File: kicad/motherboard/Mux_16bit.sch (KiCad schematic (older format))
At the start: 13 parts, among them U1 SN74ALVC00, U10 SN74ALVC00, U11 SN74ALVC00, U12 SN74ALVC00, U13 SN74ALVC00, U2 SN74ALVC00, U3 SN74ALVC00, U4 SN74ALVC00, U5 SN74ALVC00, U6 SN74ALVC00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

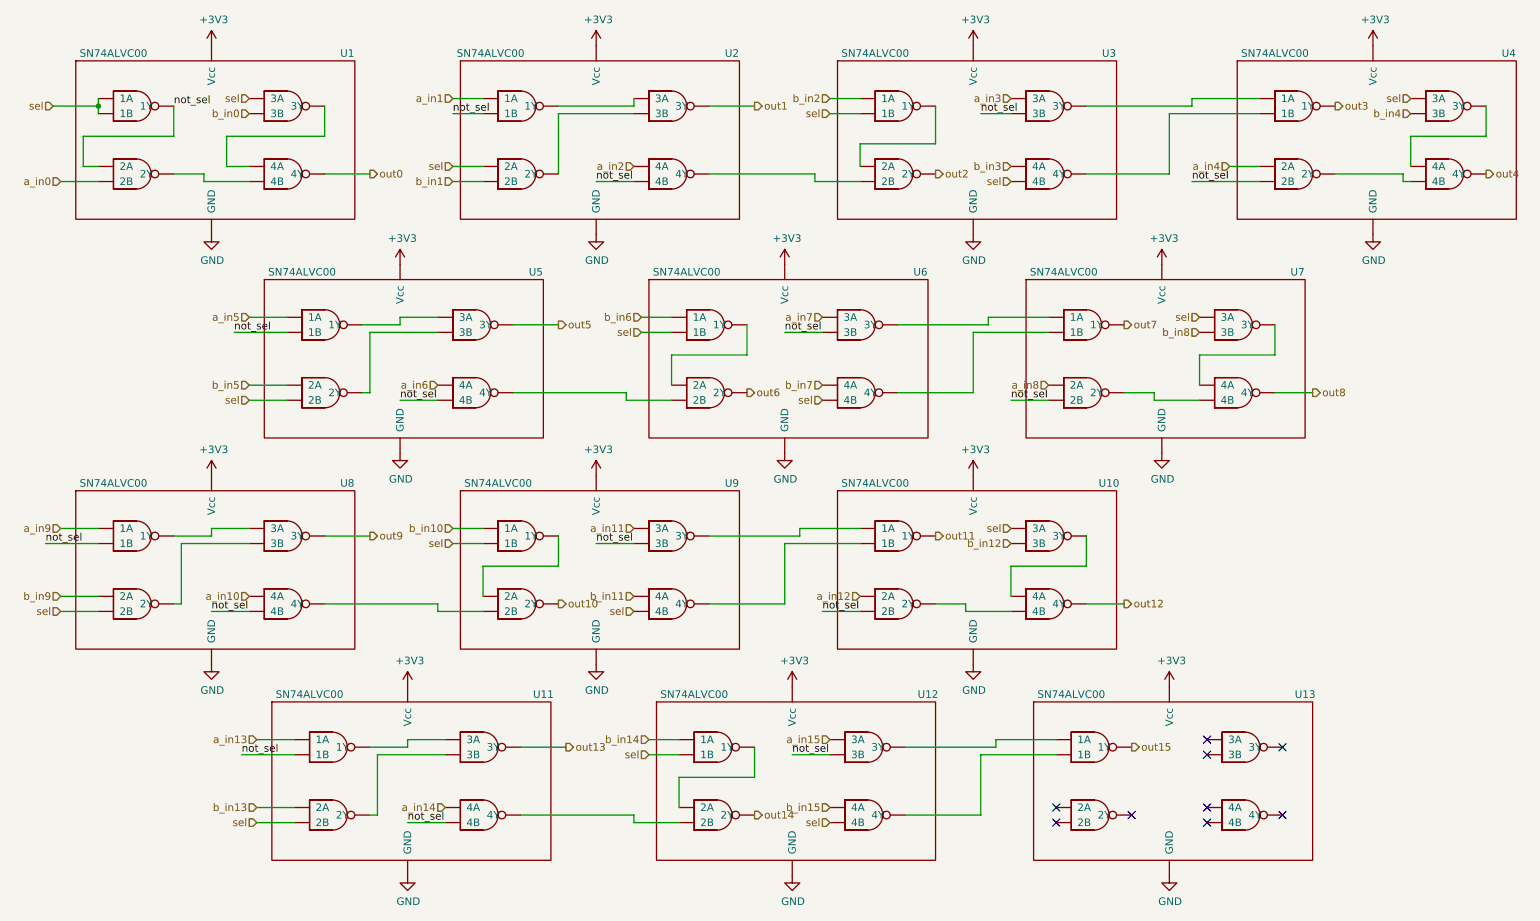
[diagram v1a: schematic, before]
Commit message: Readme updates (#6)
* Readme intro section

* Board revisions for manufacturing, add digikey PNs to all, added logo.
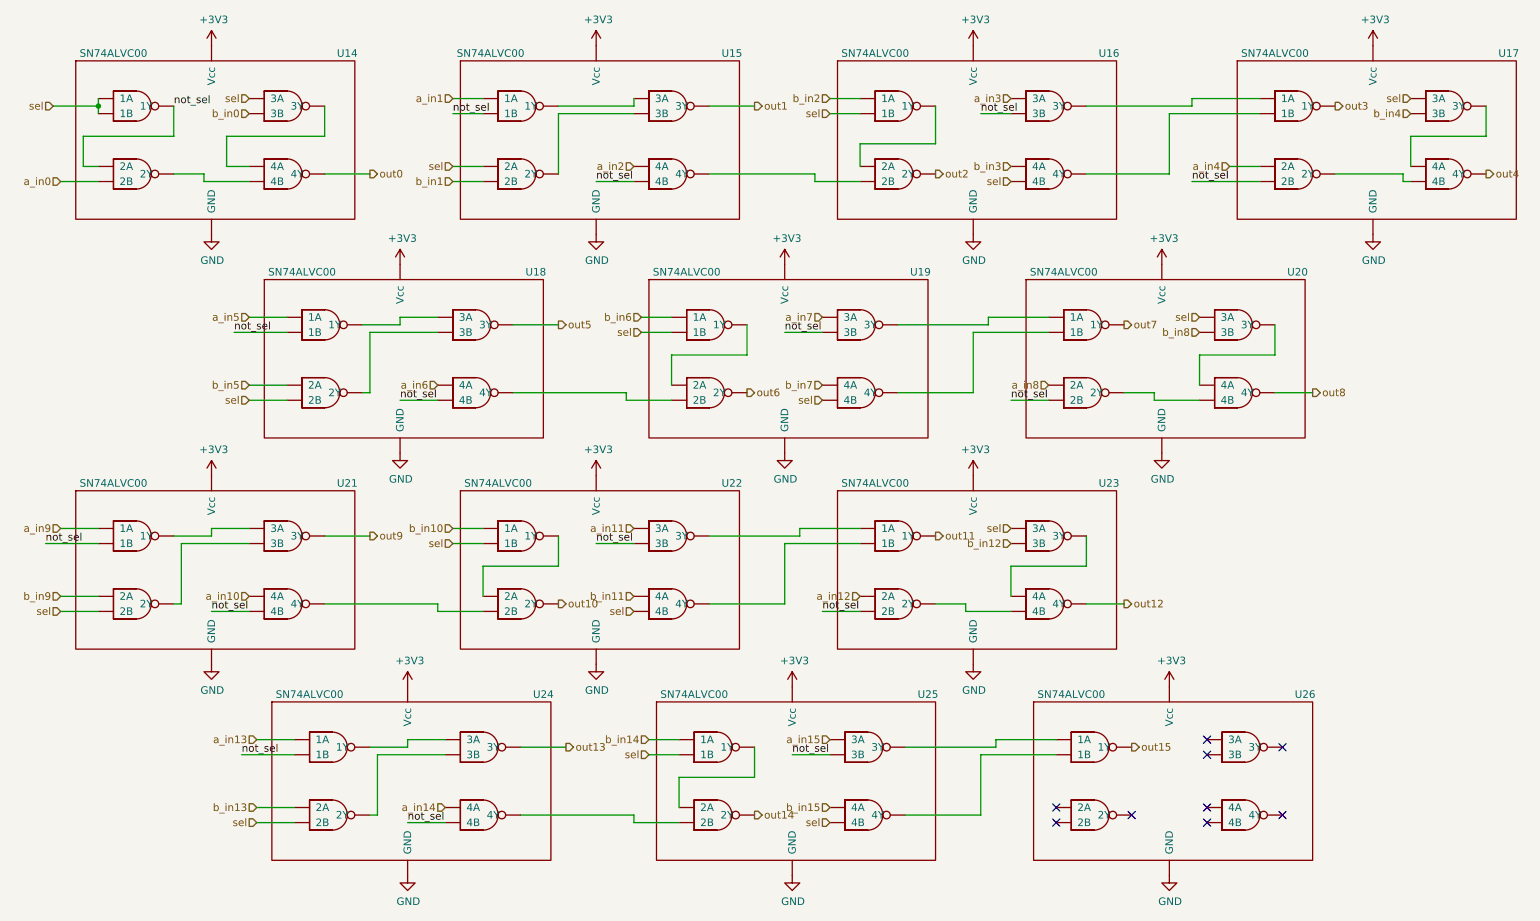
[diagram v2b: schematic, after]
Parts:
- U1, U10, U11, U12, U13, U2, U3, U4, U5, U6, U7, U8, U9: Digikey PN (none) -> 296-5104-1-ND
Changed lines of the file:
@@
 $Descr A4 11693 8268
 encoding utf-8
-Sheet 2 4
+Sheet 3 4
 Title ""
 Date ""
@@
 AR Path="/5E81995D/5E860E76" Ref="U7"  Part="1"
 AR Path="/5EAF9122/5E860E76" Ref="U20"  Part="1"
-F 0 "U7" H 9100 1600 50  0000 C CNN
+F 0 "U20" H 9100 1600 50  0000 C CNN
 F 1 "SN74ALVC00" H 7550 1600 50  0000 C CNN
 F 2 "Package_SO:TSSOP-14_4.4x5mm_P0.65mm" H 8200 450 50  0001 C CNN
 F 3 "" H 8450 1950 50  0001 C CNN
+F 4 "296-5104-1-ND" H 0   0   50  0001 C CNN "Digikey PN"
 	1    8450 1950
 	1    0    0    -1
@@
 AR Path="/5E81995D/5E85FB96" Ref="U6"  Part="1"
 AR Path="/5EAF9122/5E85FB96" Ref="U19"  Part="1"
-F 0 "U6" H 6600 1600 50  0000 C CNN
+F 0 "U19" H 6600 1600 50  0000 C CNN
 F 1 "SN74ALVC00" H 5050 1600 50  0000 C CNN
 F 2 "Package_SO:TSSOP-14_4.4x5mm_P0.65mm" H 5700 450 50  0001 C CNN
 F 3 "" H 5950 1950 50  0001 C CNN
+F 4 "296-5104-1-ND" H 0   0   50  0001 C CNN "Digikey PN"
 	1    5950 1950
 	1    0    0    -1
@@
 AR Path="/5E81995D/5E85D974" Ref="U5"  Part="1"
 AR Path="/5EAF9122/5E85D974" Ref="U18"  Part="1"
-F 0 "U5" H 4050 1600 50  0000 C CNN
+F 0 "U18" H 4050 1600 50  0000 C CNN
 F 1 "SN74ALVC00" H 2500 1600 50  0000 C CNN
 F 2 "Package_SO:TSSOP-14_4.4x5mm_P0.65mm" H 3150 450 50  0001 C CNN
 F 3 "" H 3400 1950 50  0001 C CNN
+F 4 "296-5104-1-ND" H 0   0   50  0001 C CNN "Digikey PN"
 	1    3400 1950
 	1    0    0    -1
@@
 AR Path="/5E81995D/5E835103" Ref="U4"  Part="1"
 AR Path="/5EAF9122/5E835103" Ref="U17"  Part="1"
-F 0 "U4" H 10500 150 50  0000 C CNN
+F 0 "U17" H 10500 150 50  0000 C CNN
 F 1 "SN74ALVC00" H 8950 150 50  0000 C CNN
 F 2 "Package_SO:TSSOP-14_4.4x5mm_P0.65mm" H 9600 -1000 50  0001 C CNN
 F 3 "" H 9850 500 50  0001 C CNN
+F 4 "296-5104-1-ND" H 0   0   50  0001 C CNN "Digikey PN"
 	1    9850 500
 	1    0    0    -1
@@
 AR Path="/5E81995D/5E82D6FB" Ref="U3"  Part="1"
 AR Path="/5EAF9122/5E82D6FB" Ref="U16"  Part="1"
-F 0 "U3" H 7850 150 50  0000 C CNN
+F 0 "U16" H 7850 150 50  0000 C CNN
 F 1 "SN74ALVC00" H 6300 150 50  0000 C CNN
 F 2 "Package_SO:TSSOP-14_4.4x5mm_P0.65mm" H 6950 -1000 50  0001 C CNN
 F 3 "" H 7200 500 50  0001 C CNN
+F 4 "296-5104-1-ND" H 0   0   50  0001 C CNN "Digikey PN"
 	1    7200 500
 	1    0    0    -1
@@
 AR Path="/5E81995D/5E827C09" Ref="U2"  Part="1"
 AR Path="/5EAF9122/5E827C09" Ref="U15"  Part="1"
-F 0 "U2" H 5350 150 50  0000 C CNN
+F 0 "U15" H 5350 150 50  0000 C CNN
 F 1 "SN74ALVC00" H 3750 150 50  0000 C CNN
 F 2 "Package_SO:TSSOP-14_4.4x5mm_P0.65mm" H 4450 -1000 50  0001 C CNN
 F 3 "" H 4700 500 50  0001 C CNN
+F 4 "296-5104-1-ND" H 0   0   50  0001 C CNN "Digikey PN"
 	1    4700 500
 	1    0    0    -1
@@
 AR Path="/5E81995D/5E81C818" Ref="U1"  Part="1"
 AR Path="/5EAF9122/5E81C818" Ref="U14"  Part="1"
-F 0 "U1" H 2800 150 50  0000 C CNN
+F 0 "U14" H 2800 150 50  0000 C CNN
 F 1 "SN74ALVC00" H 1250 150 50  0000 C CNN
 F 2 "Package_SO:TSSOP-14_4.4x5mm_P0.65mm" H 1900 -1000 50  0001 C CNN
 F 3 "" H 2150 500 50  0001 C CNN
+F 4 "296-5104-1-ND" H 0   0   50  0001 C CNN "Digikey PN"
 	1    2150 500
 	1    0    0    -1
@@
 AR Path="/5E81995D/5E98838F" Ref="U10"  Part="1"
 AR Path="/5EAF9122/5E98838F" Ref="U23"  Part="1"
-F 0 "U10" H 7850 3000 50  0000 C CNN
+F 0 "U23" H 7850 3000 50  0000 C CNN
 F 1 "SN74ALVC00" H 6300 3000 50  0000 C CNN
 F 2 "Package_SO:TSSOP-14_4.4x5mm_P0.65mm" H 6950 1850 50  0001 C CNN
 F 3 "" H 7200 3350 50  0001 C CNN
+F 4 "296-5104-1-ND" H 0   0   50  0001 C CNN "Digikey PN"
 	1    7200 3350
 	1    0    0    -1
@@
 AR Path="/5E81995D/5E988395" Ref="U9"  Part="1"
 AR Path="/5EAF9122/5E988395" Ref="U22"  Part="1"
-F 0 "U9" H 5350 3000 50  0000 C CNN
+F 0 "U22" H 5350 3000 50  0000 C CNN
 F 1 "SN74ALVC00" H 3800 3000 50  0000 C CNN
 F 2 "Package_SO:TSSOP-14_4.4x5mm_P0.65mm" H 4450 1850 50  0001 C CNN
 F 3 "" H 4700 3350 50  0001 C CNN
+F 4 "296-5104-1-ND" H 0   0   50  0001 C CNN "Digikey PN"
 	1    4700 3350
 	1    0    0    -1
@@
 AR Path="/5E81995D/5E98839B" Ref="U8"  Part="1"
 AR Path="/5EAF9122/5E98839B" Ref="U21"  Part="1"
-F 0 "U8" H 2800 3000 50  0000 C CNN
+F 0 "U21" H 2800 3000 50  0000 C CNN
 F 1 "SN74ALVC00" H 1250 3000 50  0000 C CNN
 F 2 "Package_SO:TSSOP-14_4.4x5mm_P0.65mm" H 1900 1850 50  0001 C CNN
 F 3 "" H 2150 3350 50  0001 C CNN
+F 4 "296-5104-1-ND" H 0   0   50  0001 C CNN "Digikey PN"
 	1    2150 3350
 	1    0    0    -1
@@
 AR Path="/5E81995D/5E990E7F" Ref="U13"  Part="1"
 AR Path="/5EAF9122/5E990E7F" Ref="U26"  Part="1"
-F 0 "U13" H 9150 4400 50  0000 C CNN
+F 0 "U26" H 9150 4400 50  0000 C CNN
 F 1 "SN74ALVC00" H 7600 4400 50  0000 C CNN
 F 2 "Package_SO:TSSOP-14_4.4x5mm_P0.65mm" H 8250 3250 50  0001 C CNN
 F 3 "" H 8500 4750 50  0001 C CNN
+F 4 "296-5104-1-ND" H 0   0   50  0001 C CNN "Digikey PN"
 	1    8500 4750
 	1    0    0    -1
@@
 AR Path="/5E81995D/5E990E85" Ref="U12"  Part="1"
 AR Path="/5EAF9122/5E990E85" Ref="U25"  Part="1"
-F 0 "U12" H 6650 4400 50  0000 C CNN
+F 0 "U25" H 6650 4400 50  0000 C CNN
 F 1 "SN74ALVC00" H 5100 4400 50  0000 C CNN
 F 2 "Package_SO:TSSOP-14_4.4x5mm_P0.65mm" H 5750 3250 50  0001 C CNN
 F 3 "" H 6000 4750 50  0001 C CNN
+F 4 "296-5104-1-ND" H 0   0   50  0001 C CNN "Digikey PN"
 	1    6000 4750
 	1    0    0    -1
@@
 AR Path="/5E81995D/5E990E8B" Ref="U11"  Part="1"
 AR Path="/5EAF9122/5E990E8B" Ref="U24"  Part="1"
-F 0 "U11" H 4100 4400 50  0000 C CNN
+F 0 "U24" H 4100 4400 50  0000 C CNN
 F 1 "SN74ALVC00" H 2550 4400 50  0000 C CNN
 F 2 "Package_SO:TSSOP-14_4.4x5mm_P0.65mm" H 3200 3250 50  0001 C CNN
 F 3 "" H 3450 4750 50  0001 C CNN
+F 4 "296-5104-1-ND" H 0   0   50  0001 C CNN "Digikey PN"
 	1    3450 4750
 	1    0    0    -1
